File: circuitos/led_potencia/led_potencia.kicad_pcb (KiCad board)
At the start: 2 copper layers, 42 parts, among them J10 Conn_01x02_Pin, J11 Conn_01x02_Pin, J12 Conn_01x02_Pin, J13 Conn_01x02_Pin, J14 Conn_01x02_Pin, J15 Conn_01x02_Pin, J16 Conn_01x02_Pin, J17 Conn_01x02_Socket, J18 Conn_01x02_Socket, J19 Conn_01x02_Socket, J20 Conn_01x05_IN, J21 Conn_01x05_OUT, J9 Conn_01x02_Pin, Q17 IRLZ44N, Q18 IRLZ44N, Q19 IRLZ44N, Q20 IRLZ44N, Q21 IRLZ44N, Q22 IRLZ44N, Q23 IRLZ44N, Q24 IRLZ44N, U1 74HC595

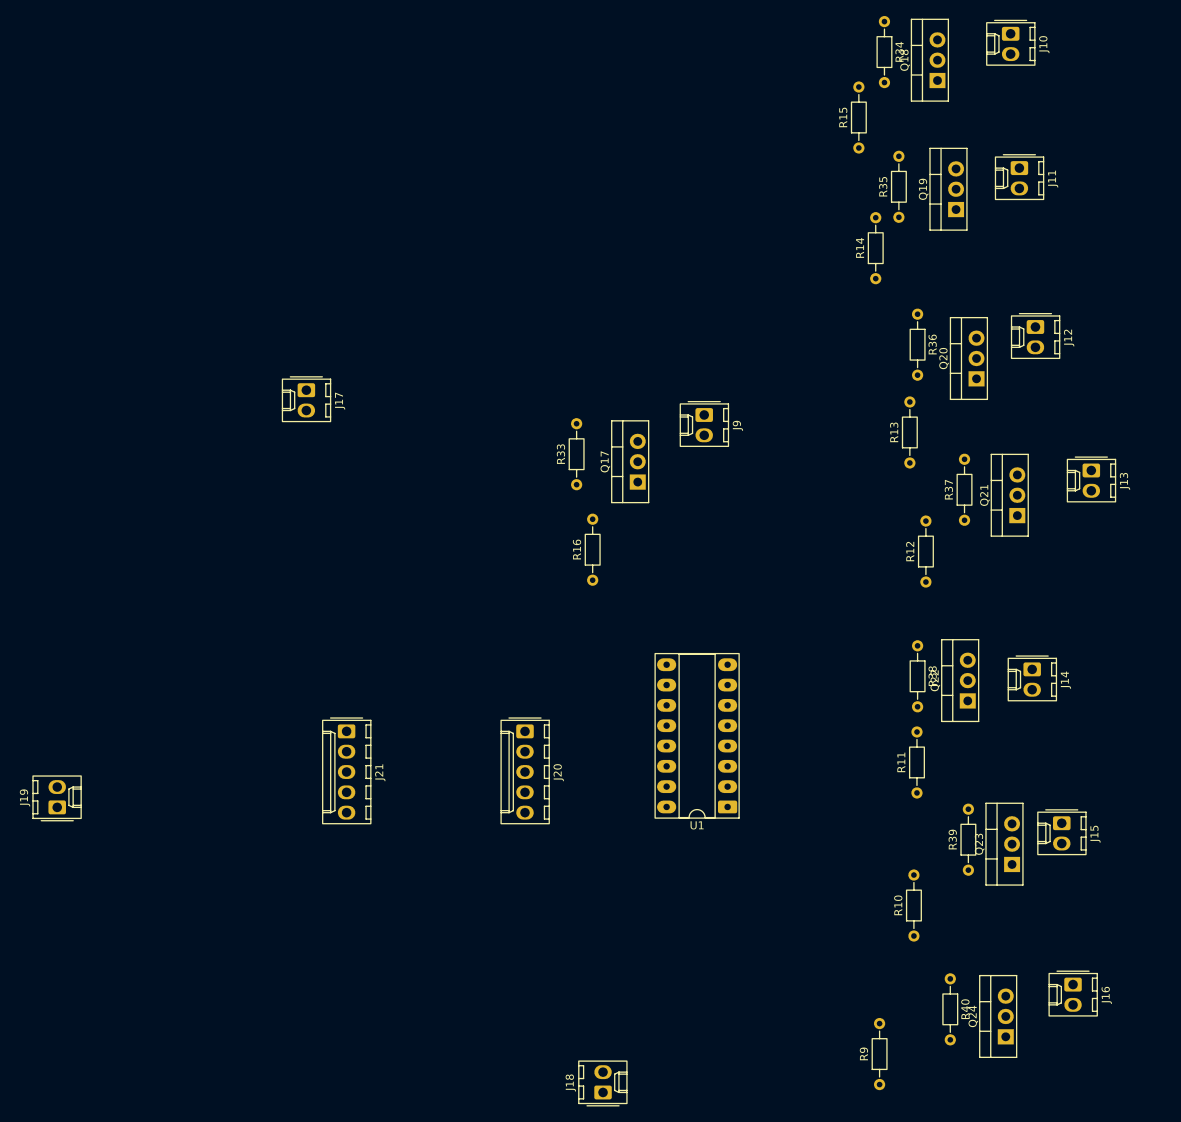
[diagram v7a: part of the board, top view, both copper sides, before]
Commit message: cambiando resistencias
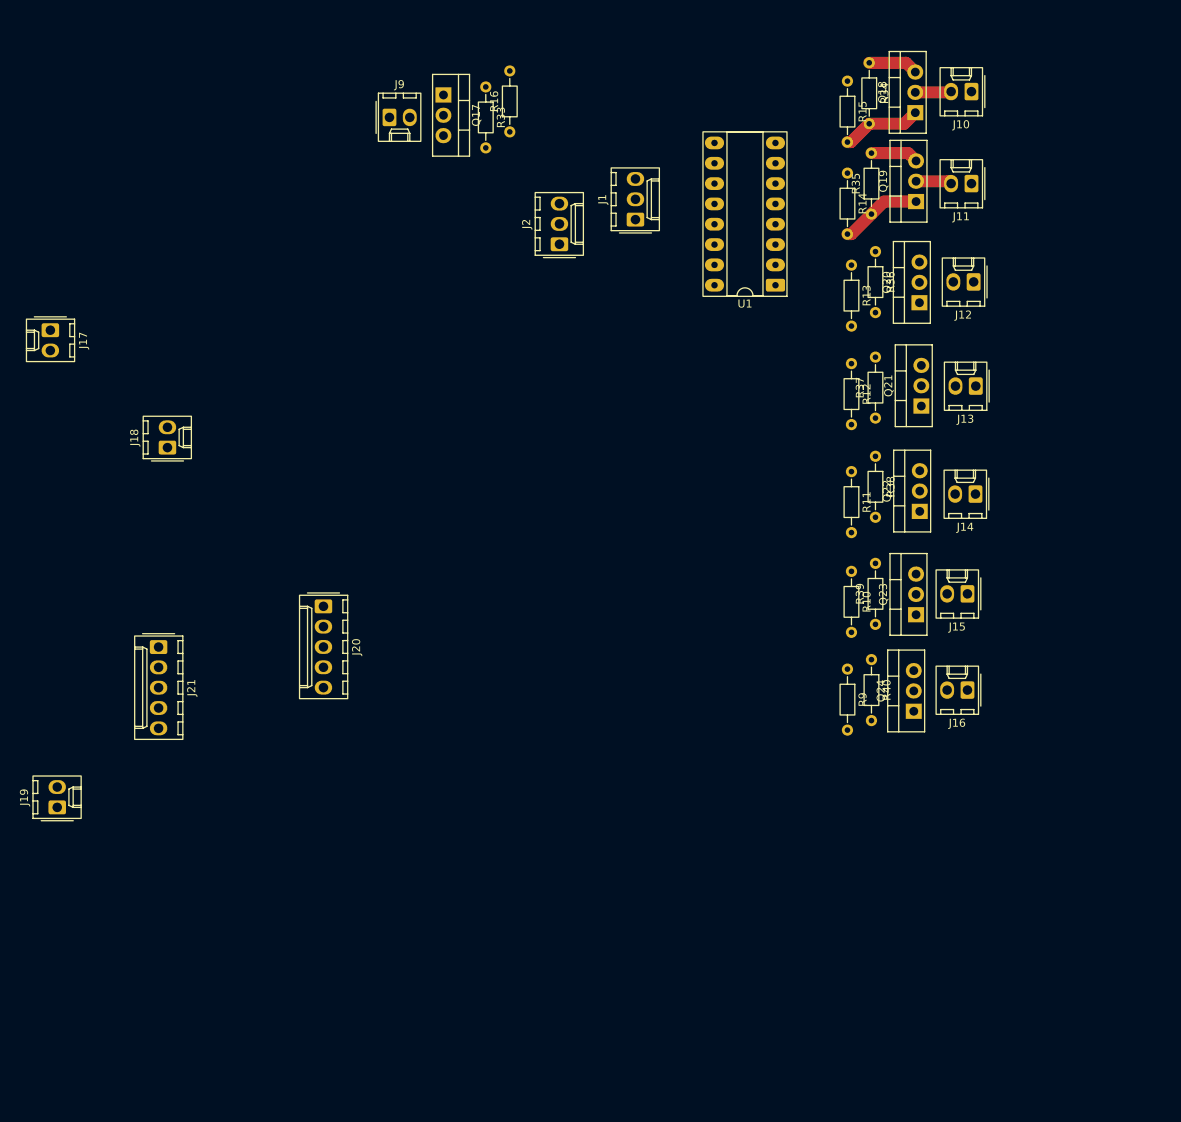
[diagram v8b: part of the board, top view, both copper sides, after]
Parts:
- added J1: Conn_01x03_Pin, Connector_Molex:Molex_KK-254_AE-6410-03A_1x03_P2.54mm_Vertical, F.Cu at (161.0, 48.5)
- added J2: Conn_01x03_Pin, Connector_Molex:Molex_KK-254_AE-6410-03A_1x03_P2.54mm_Vertical, F.Cu at (151.5, 51.6)
- R10, R11, R12, R13, R14, R15, R16, R9: value 1k -> 220
- moved J18 97.3 mm to (102.5, 77.0)
- moved U1 65.5 mm to (178.5, 56.7)
- moved R16 57.0 mm to (145.3, 37.5)
- moved J9 54.1 mm to (130.2, 35.7), turned to 0 degrees
- moved Q17 54.1 mm to (137.0, 32.9), turned to -90 degrees
- moved R9 52.1 mm to (187.5, 104.7), turned to -90 degrees
- moved R33 51.0 mm to (142.3, 31.9), turned to -90 degrees
- moved R10 46.2 mm to (188.0, 92.5), turned to -90 degrees
- moved Q24 42.3 mm to (195.8, 110.0)
- moved R40 41.1 mm to (190.5, 103.5)
- moved R11 41.0 mm to (188.0, 80.0), turned to -90 degrees
- moved J16 39.1 mm to (202.5, 107.3), turned to 180 degrees
- moved Q23 33.4 mm to (196.1, 97.9)
- moved J17 32.9 mm to (87.9, 62.3)
- moved R39 32.8 mm to (191.0, 99.1)
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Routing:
- net GND: track 0.00 -> 12.2 mm
- net Net-(Q19-G): track 0.00 -> 10.3 mm
- net Net-(Q18-G): track 0.00 -> 10.0 mm
- net Net-(J10-Pin_2): track 0.00 -> 4.52 mm
- net Net-(J11-Pin_2): track 0.00 -> 4.51 mm
